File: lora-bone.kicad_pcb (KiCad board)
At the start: 2 copper layers, 30 x 100 mm, 23 parts, among them J1 Analog IN, J10 GS2, J11 GS2, J12 GS2, J13 GS2, J15 CONN_COAXIAL, J2 POWER, J3 Bluepill left, J4 PWM OUT, J5 SPI OUT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

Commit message: More Labeles for Breakout Header
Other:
- board text added: "5 3V3 GND GND"
- board text added: "A0 A1 A2 GND"
- board text added: "GND A2 A1 A0"
- board text added: "GND GND 3V3 5"
- board text added: "GND RX TX"
- board text added: "PB11 PB10 PB9 PB8"
- board text added: "PB13 PB14 PB15"
- board text added: "PB15 PB14 PB13"
- board text added: "PB8 PB9 PB10 PB11"
- board text added: "TX RX GND"
- board text added: "UART"
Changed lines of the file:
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@@
     (area 29.924999 49.924999 60.075001 150.075001)
     (thickness 1.6)
-    (drawings 22)
+    (drawings 33)
     (tracks 462)
     (zones 0)
@@
     (descr "Through hole straight pin header, 1x04, 2.54mm pitch, single row")
     (tags "Through hole pin header THT 1x04 2.54mm single row")
-    (fp_text reference J2 (at 0 -2.33 180) (layer F.SilkS)
+    (fp_text reference J2 (at 0 -2.33 180) (layer F.SilkS) hide
       (effects (font (size 1 1) (thickness 0.15)))
     )
@@
     (descr "Through hole straight pin header, 1x04, 2.54mm pitch, single row")
     (tags "Through hole pin header THT 1x04 2.54mm single row")
-    (fp_text reference J8 (at 0 -2.33) (layer F.SilkS)
+    (fp_text reference J8 (at 0 -2.33) (layer F.SilkS) hide
       (effects (font (size 1 1) (thickness 0.15)))
     )
@@
     (descr "Through hole straight pin header, 1x04, 2.54mm pitch, single row")
     (tags "Through hole pin header THT 1x04 2.54mm single row")
-    (fp_text reference J1 (at 0 -2.33) (layer F.SilkS)
+    (fp_text reference J1 (at 0 -2.33) (layer F.SilkS) hide
       (effects (font (size 1 1) (thickness 0.15)))
     )
@@
     (descr "Through hole straight pin header, 1x03, 2.54mm pitch, single row")
     (tags "Through hole pin header THT 1x03 2.54mm single row")
-    (fp_text reference J4 (at 0 -2.33 180) (layer F.SilkS)
+    (fp_text reference J4 (at 0 -2.33 180) (layer F.SilkS) hide
       (effects (font (size 1 1) (thickness 0.15)))
     )
@@
     (descr "Through hole straight pin header, 1x04, 2.54mm pitch, single row")
     (tags "Through hole pin header THT 1x04 2.54mm single row")
-    (fp_text reference J5 (at 0 -2.33 180) (layer F.SilkS)
+    (fp_text reference J5 (at 0 -2.33 180) (layer F.SilkS) hide
       (effects (font (size 1 1) (thickness 0.15)))
     )
@@
     (descr "Through hole straight pin header, 1x04, 2.54mm pitch, single row")
     (tags "Through hole pin header THT 1x04 2.54mm single row")
-    (fp_text reference J7 (at 0 -2.33) (layer F.SilkS)
+    (fp_text reference J7 (at 0 -2.33) (layer F.SilkS) hide
       (effects (font (size 1 1) (thickness 0.15)))
     )
@@
     (descr "Through hole straight pin header, 1x03, 2.54mm pitch, single row")
     (tags "Through hole pin header THT 1x03 2.54mm single row")
-    (fp_text reference J9 (at 0 -2.33 180) (layer F.SilkS)
+    (fp_text reference J9 (at 0 -2.33 180) (layer F.SilkS) hide
       (effects (font (size 1 1) (thickness 0.15)))
     )
@@
     (pad 1 thru_hole circle (at 0 0) (size 3.2 3.2) (drill 3.2) (layers *.Cu *.Mask))
   )
+  (gr_text UART (at 58.166 122.682 90) (layer F.SilkS)
+    (effects (font (size 1.5 1.5) (thickness 0.3)))
+  )
+  (gr_text "5 3V3 GND GND" (at 55.372 101.092 90) (layer F.SilkS)
+    (effects (font (size 0.75 0.75) (thickness 0.1875)))
+  )
+  (gr_text "GND GND 3V3 5" (at 55.372 101.092 90) (layer B.SilkS)
+    (effects (font (size 0.75 0.75) (thickness 0.1875)) (justify mirror))
+  )
+  (gr_text "GND  A2  A1  A0" (at 34.544 111.76 270) (layer B.SilkS)
+    (effects (font (size 0.75 0.75) (thickness 0.1875)) (justify mirror))
+  )
+  (gr_text "A0  A1  A2  GND" (at 34.544 111.76 270) (layer F.SilkS)
+    (effects (font (size 0.75 0.75) (thickness 0.1875)))
+  )
+  (gr_text "PB11 PB10 PB9 PB8" (at 34.544 132.334 270) (layer B.SilkS)
+    (effects (font (size 0.75 0.75) (thickness 0.1875)) (justify mirror))
+  )
+  (gr_text "PB8 PB9 PB10 PB11" (at 34.544 132.334 270) (layer F.SilkS)
+    (effects (font (size 0.75 0.75) (thickness 0.1875)))
+  )
+  (gr_text "GND RX TX" (at 55.372 129.794 90) (layer B.SilkS)
+    (effects (font (size 0.75 0.75) (thickness 0.1875)) (justify mirror))
+  )
+  (gr_text "TX RX GND" (at 55.372 129.794 90) (layer F.SilkS)
+    (effects (font (size 0.75 0.75) (thickness 0.1875)))
+  )
+  (gr_text "PB15 PB14 PB13" (at 55.372 139.446 90) (layer B.SilkS)
+    (effects (font (size 0.75 0.75) (thickness 0.1875)) (justify mirror))
+  )
+  (gr_text "PB13 PB14 PB15" (at 55.372 139.446 90) (layer F.SilkS)
+    (effects (font (size 0.75 0.75) (thickness 0.1875)))
+  )
   (gr_text SPI (at 58.674 86.106 90) (layer F.SilkS)

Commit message: A few little corrections
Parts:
- renumbered J15 to ANT1
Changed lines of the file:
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@@
   (net 40 "Net-(J3-Pad17)")
   (net 41 "Net-(J6-Pad20)")
-  (net 42 "Net-(J15-Pad1)")
+  (net 42 "Net-(ANT1-Pad1)")
   (net_class Default "This is the default net class."
     (clearance 0.2)
@@
     (add_net MISO)
     (add_net MOSI)
-    (add_net "Net-(J15-Pad1)")
+    (add_net "Net-(ANT1-Pad1)")
     (add_net "Net-(J3-Pad1)")
     (add_net "Net-(J3-Pad13)")
@@
     (descr "Mounting Hole 3.2mm, no annular, M3, ISO14580")
     (tags "mounting hole 3.2mm no annular m3 iso14580")
-    (fp_text reference REF** (at 0 -3.75) (layer F.SilkS)
+    (fp_text reference REF** (at 0 -3.75) (layer F.SilkS) hide
       (effects (font (size 1 1) (thickness 0.15)))
     )
@@
     (descr "SMA pcb through hole jack")
     (tags "SMA THT Jack Straight")
-    (fp_text reference J15 (at 5.334 0) (layer F.SilkS)
+    (fp_text reference ANT1 (at 5.334 0) (layer F.SilkS)
       (effects (font (size 1 1) (thickness 0.15)))
     )
@@
       (net 3 GND))
     (pad 1 thru_hole circle (at 0 0) (size 2 2) (drill 1.5) (layers *.Cu *.Mask)
-      (net 42 "Net-(J15-Pad1)"))
+      (net 42 "Net-(ANT1-Pad1)"))
   )
   (module Capacitors_SMD:C_0805_HandSoldering (layer F.Cu)
@@
     (tags "capacitor 0805")
     (attr smd)
-    (fp_text reference C1 (at 0 -1.75 90) (layer F.SilkS)
+    (fp_text reference C1 (at -3.556 0 90) (layer F.SilkS)
       (effects (font (size 1 1) (thickness 0.15)))
     )
@@
       (net 3 GND))
     (pad 9 smd rect (at 7 -1 180) (size 3.1 1.2) (drill (offset 1 0)) (layers F.Cu F.Paste F.Mask)
-      (net 42 "Net-(J15-Pad1)"))
+      (net 42 "Net-(ANT1-Pad1)"))
     (pad 8 smd rect (at -7 -1 180) (size 3.1 1.2) (drill (offset -1 0)) (layers F.Cu F.Paste F.Mask)
       (net 3 GND))
@@
     (descr "Mounting Hole 3.2mm, no annular, M3, ISO14580")
     (tags "mounting hole 3.2mm no annular m3 iso14580")
-    (fp_text reference REF** (at 0 -3.75) (layer F.SilkS)
-      (effects (font (size 1 1) (thickness 0.15)))
-    )
+    (fp_text reference REF** (at 0 -3.75) (layer F.SilkS) hide
+      (effects (font (size 1 1) (thickness 0.15)))
+    )

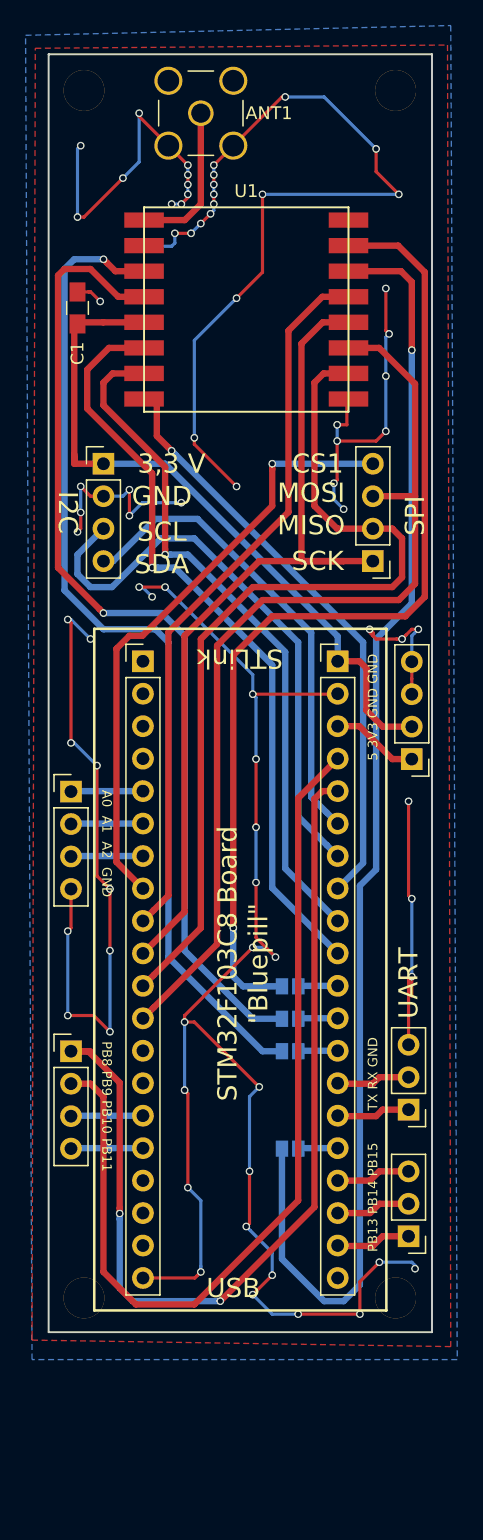
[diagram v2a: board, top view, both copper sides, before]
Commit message: Nicer Ground Planes, nicer Via placements, hopefully better Ground Distribution :>
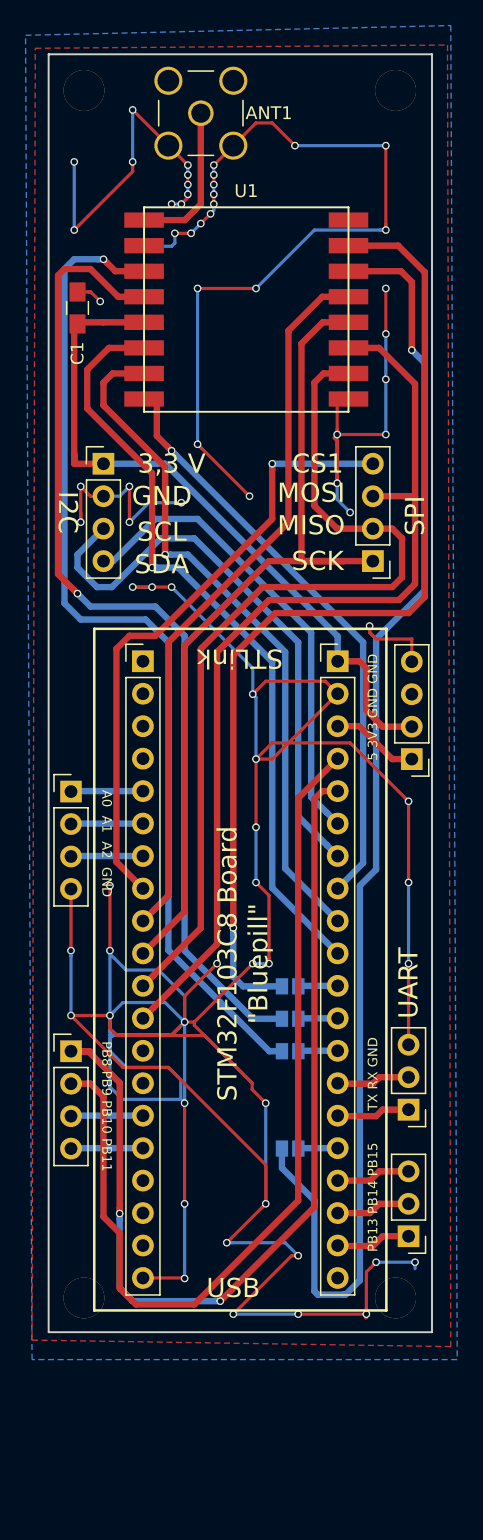
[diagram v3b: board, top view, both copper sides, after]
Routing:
- net GND: track 337.8 -> 435.9 mm, vias 78 -> 71
- net CS1: track 47.6 -> 48.2 mm

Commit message: More Logos.
There can never be enough logos. It is not possible to reduce the count of Logos
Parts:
- removed the G*** at (44.5, 92.5)
- added G***: LOGO, LOGO, B.Cu at (45.5, 89.9)
- added G***: LOGO, LOGO, B.Cu at (43.9, 138.9)
- moved G*** 3.59 mm to (43.4, 109.0)
- moved G*** 1.55 mm to (46.7, 69.8)
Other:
- board text added: "SWCLK"
- board text added: "SWDIO"
- board text added: "U23 Projekt 2017"

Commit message: A few changes and corrections
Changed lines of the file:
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@@
   (page A4)
   (layers
-    (0 F.Cu signal hide)
-    (31 B.Cu signal hide)
+    (0 F.Cu signal)
+    (31 B.Cu signal)
     (32 B.Adhes user)
     (33 F.Adhes user)
@@
   )
   (setup
-    (last_trace_width 1)
+    (last_trace_width 0.25)
     (user_trace_width 0.5)
     (user_trace_width 1)
@@
     )
   )
+  (module Mounting_Holes:MountingHole_3.2mm_M3_ISO14580 (layer F.Cu)
+    (at 57.15 52.832)
+    (descr "Mounting Hole 3.2mm, no annular, M3, ISO14580")
+    (tags "mounting hole 3.2mm no annular m3 iso14580")
+    (fp_text reference REF** (at 0 -3.75) (layer F.SilkS) hide
+      (effects (font (size 1 1) (thickness 0.15)))
+    )
+    (fp_text value MountingHole_3.2mm_M3_ISO14580 (at 0 3.75) (layer F.Fab)
+      (effects (font (size 1 1) (thickness 0.15)))
+    )
+    (fp_circle (center 0 0) (end 2.75 0) (layer Cmts.User) (width 0.15))
+    (fp_circle (center 0 0) (end 3 0) (layer F.CrtYd) (width 0.05))
+    (pad 1 thru_hole circle (at 0 0) (size 3.2 3.2) (drill 3.2) (layers *.Cu *.Mask))
+  )
   (module RFM95W:RFM95W_SMD (layer F.Cu)
     (at 45.466 61.976 180)
@@
     )
     (fp_line (start -8 0) (end 8 0) (layer F.SilkS) (width 0.15))
-    (fp_line (start -8 -16) (end -8 0) (layer F.SilkS) (width 0.15))
     (fp_line (start 8 -16) (end -8 -16) (layer F.SilkS) (width 0.15))
-    (fp_line (start 8 0) (end 8 -16) (layer F.SilkS) (width 0.15))
     (pad 16 smd rect (at 7 -15 180) (size 3.1 1.2) (drill (offset 1 0)) (layers F.Cu F.Paste F.Mask)
       (net 21 DIO2))
@@
     (pad 1 smd rect (at -7 -15 180) (size 3.1 1.2) (drill (offset -1 0)) (layers F.Cu F.Paste F.Mask)
       (net 3 GND))
-  )
-  (module Mounting_Holes:MountingHole_3.2mm_M3_ISO14580 (layer F.Cu)
-    (at 57.15 52.832)
-    (descr "Mounting Hole 3.2mm, no annular, M3, ISO14580")
-    (tags "mounting hole 3.2mm no annular m3 iso14580")
-    (fp_text reference REF** (at 0 -3.75) (layer F.SilkS) hide
-      (effects (font (size 1 1) (thickness 0.15)))
-    )
-    (fp_text value MountingHole_3.2mm_M3_ISO14580 (at 0 3.75) (layer F.Fab)
-      (effects (font (size 1 1) (thickness 0.15)))
-    )
-    (fp_circle (center 0 0) (end 2.75 0) (layer Cmts.User) (width 0.15))
-    (fp_circle (center 0 0) (end 3 0) (layer F.CrtYd) (width 0.05))
-    (pad 1 thru_hole circle (at 0 0) (size 3.2 3.2) (drill 3.2) (layers *.Cu *.Mask))
   )
   (gr_text "U23 Projekt\n2017" (at 57.658 67.818 90) (layer F.SilkS)
@@
     (polygon
       (pts
-        (xy 28.702 150.368) (xy 28.956 49.53) (xy 61.214 49.276) (xy 61.468 151.13) (xy 28.702 150.622)
+        (xy 29.972 149.86) (xy 29.972 50.038) (xy 59.944 50.038) (xy 59.944 149.86)
       )
     )
@@
     (polygon
       (pts
-        (xy 28.702 152.146) (xy 28.194 48.514) (xy 61.468 47.752) (xy 61.976 152.146)
+        (xy 29.972 149.86) (xy 29.972 50.038) (xy 59.944 50.038) (xy 59.944 149.86)
       )
     )

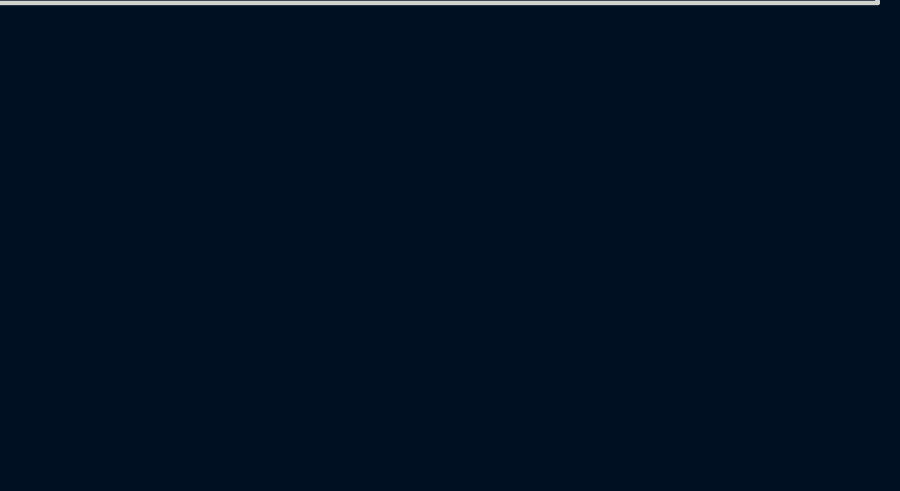
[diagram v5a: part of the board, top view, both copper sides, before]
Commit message: Add power GPIO hint
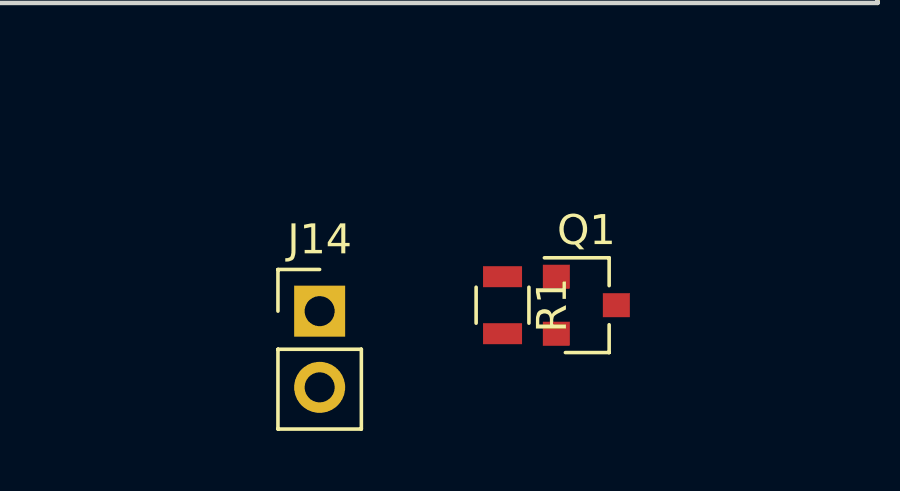
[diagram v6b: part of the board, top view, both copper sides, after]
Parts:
- added J14: CONN_01X02, Pin_Headers:Pin_Header_Straight_1x02_Pitch2.54mm, F.Cu at (41.4, 160.3)
- added Q1: 2N7002, TO_SOT_Packages_SMD:SOT-23, F.Cu at (50.3, 160.1)
- added R1: 100k, Resistors_SMD:R_0805, F.Cu at (47.5, 160.1)
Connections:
- J3 pad 1: Net-(J3-Pad1) -> (no net)
- J3 pad 13: Net-(J3-Pad13) -> (no net)
- J3 pad 14: Net-(J3-Pad14) -> (no net)
- J3 pad 17: Net-(J3-Pad17) -> (no net)
- J3 pad 2: Net-(J3-Pad2) -> (no net)
- J3 pad 3: Net-(J3-Pad3) -> (no net)
- J3 pad 4: Net-(J3-Pad4) -> (no net)
- J6 pad 20: Net-(J6-Pad20) -> (no net)

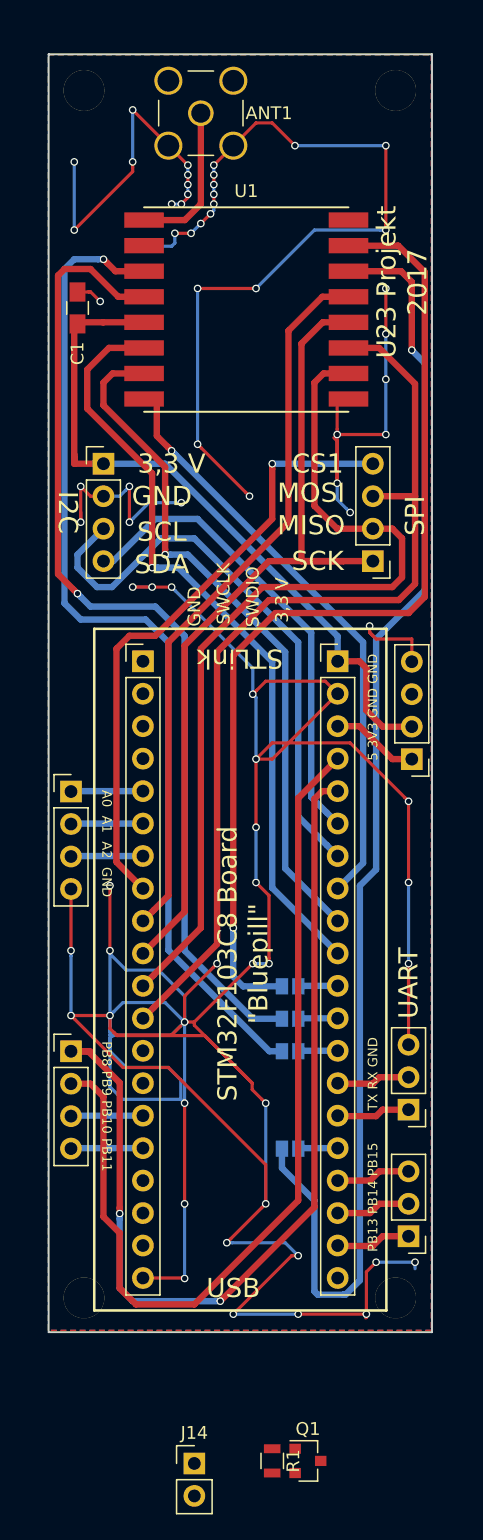
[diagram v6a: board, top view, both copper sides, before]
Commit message: Power GPIO routet. Added Pull UP Resistor for PB8
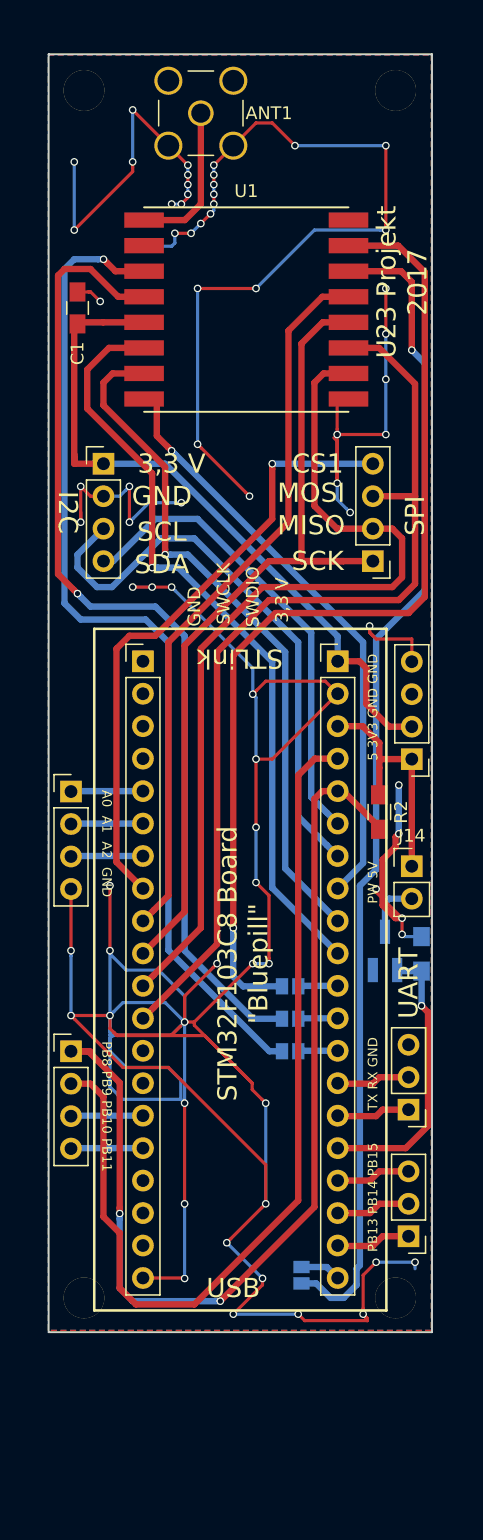
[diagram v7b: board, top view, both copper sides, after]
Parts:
- added R2: 5k, Resistors_SMD:R_0805_HandSoldering, F.Cu at (55.9, 109.3)
- J14: value CONN_01X02 -> POWER OUT
- Q1: footprint TO_SOT_Packages_SMD:SOT-23 -> TO_SOT_Packages_SMD:SOT-23_Handsoldering; moved to B.Cu
- R1: footprint Resistors_SMD:R_0805 -> Resistors_SMD:R_0805_HandSoldering; moved to B.Cu
- moved J14 49.7 mm to (58.4, 113.5)
- moved R1 41.4 mm to (59.2, 120.4), turned to 90 degrees
- moved Q1 40.4 mm to (56.3, 120.2), turned to 90 degrees
- moved J13 9.95 mm to (49.8, 145.5), turned to 0 degrees
- moved G*** 4.58 mm to (44.2, 134.4)
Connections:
- J13 pad 2: PA8 -> PB12
- J3 pad 1: (no net) -> Net-(J3-Pad1)
- J3 pad 13: (no net) -> Net-(J3-Pad13)
- J3 pad 14: (no net) -> Net-(J3-Pad14)
- J3 pad 17: (no net) -> Net-(J3-Pad17)
- J3 pad 2: (no net) -> Net-(J3-Pad2)
- J3 pad 3: (no net) -> Net-(J3-Pad3)
- J3 pad 4: (no net) -> Net-(J3-Pad4)
- J6 pad 20: (no net) -> PB12
- Q1 pad 1: Net-(Q1-Pad1) -> PA8
- R1 pad 1: Net-(Q1-Pad1) -> PA8
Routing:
- net GND: track 435.9 -> 413.5 mm, vias 71 -> 73
- net PA8: track 3.09 -> 22.1 mm, vias 0 -> 1
- net +5V: track 6.87 -> 18.8 mm
- net RESET: track 103.3 -> 92.6 mm
- net Net-(J14-Pad2): track 0.00 -> 4.86 mm
- net PB8: track 75.2 -> 79.9 mm
- net PB12: track 0.00 -> 3.19 mm
- net PB9: track 72.2 -> 73.2 mm
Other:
- board text added: "5V PW"
- board text added: "PW 5V"
